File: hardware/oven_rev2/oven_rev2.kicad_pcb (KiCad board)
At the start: 2 copper layers, 54.6 x 108 mm, 22 parts, among them J1 RELAY_CTRL, J10 5V_IN, J2 SERIAL, J3 NUMPAD, J4 AVR-ISP-6, J5 LIVE, J6 DISPLAY, J7 RELAY_PWR, J8 OUTPUT, J9 NEUTRAL, U1 ATmega328-AU, U2 MAX6675, Y1 16M

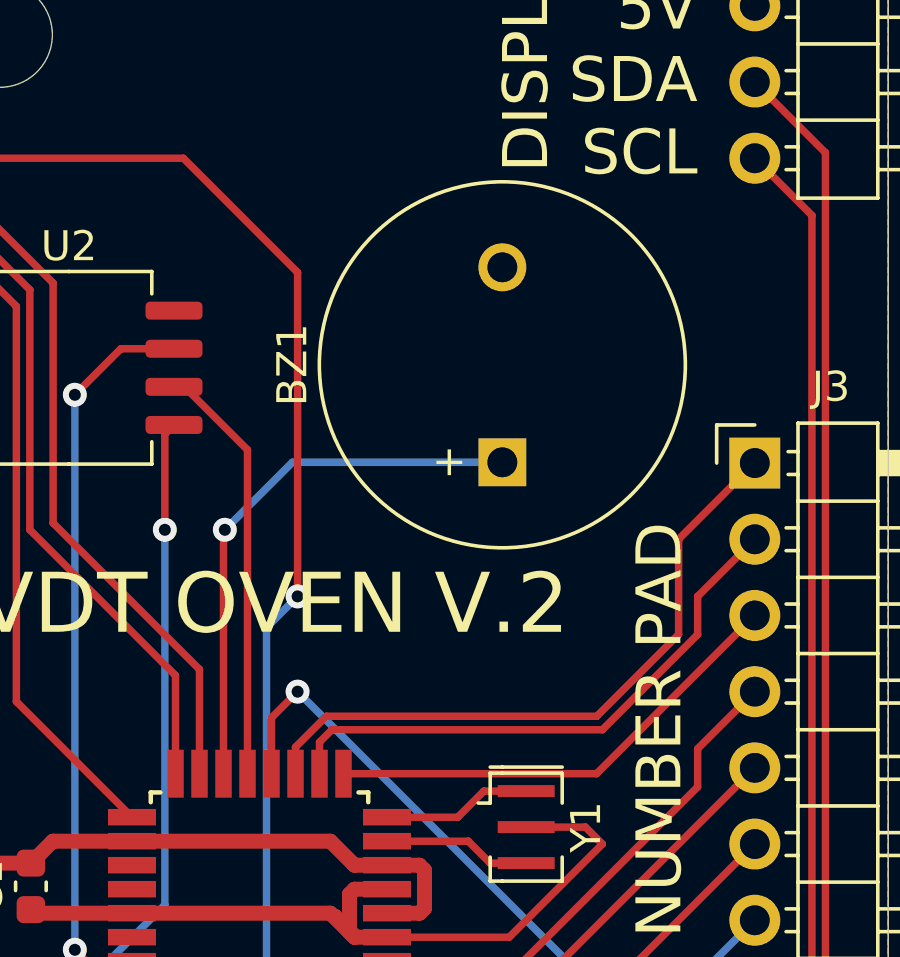
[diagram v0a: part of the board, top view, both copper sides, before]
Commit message: Removed buzzer that was not present in fabricated boards
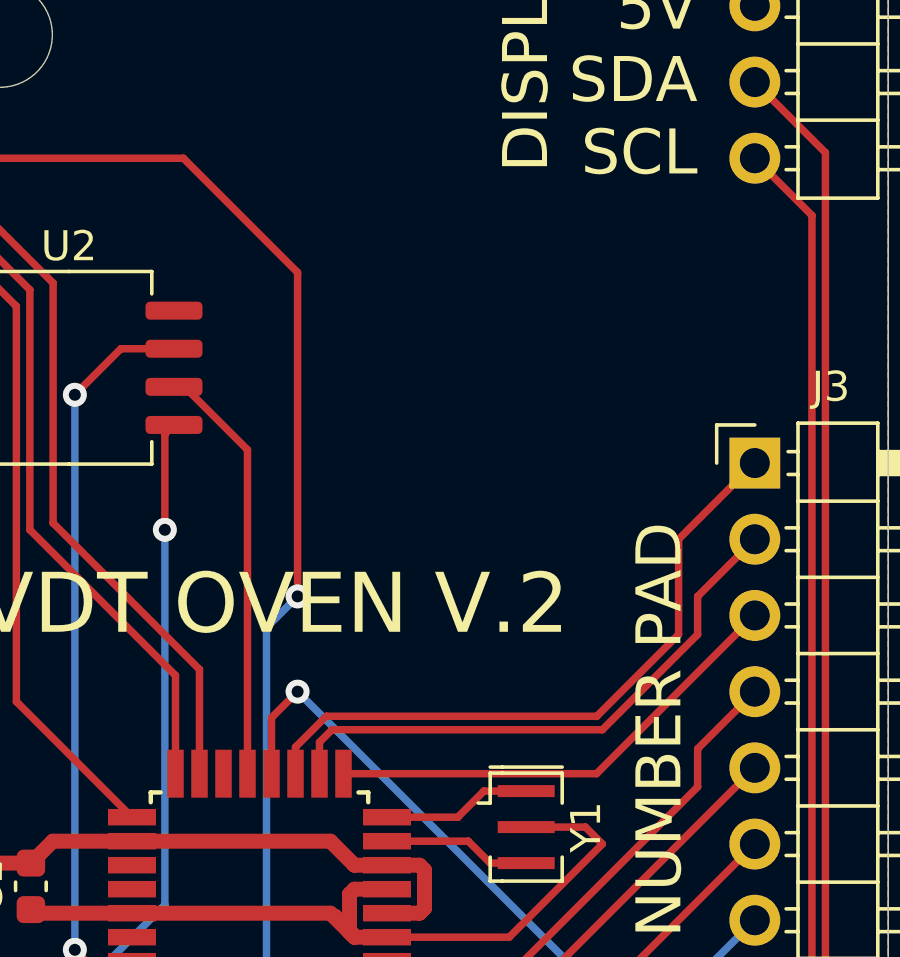
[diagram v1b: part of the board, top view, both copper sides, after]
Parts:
- removed BZ1: AT1224TWT, Buzzer_Beeper:MagneticBuzzer_ProSignal_ABT-410-RC
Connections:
- net /COL_{3 renamed /COL_{3}
- U1 pad 14: /BUZZ -> unconnected-(U1-PB2-Pad14)
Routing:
- net /BUZZ: track 18.3 -> 0.00 mm, vias 1 -> 0
